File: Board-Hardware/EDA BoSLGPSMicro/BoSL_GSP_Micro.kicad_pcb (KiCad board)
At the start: 2 copper layers, 88 x 69.8 mm, 58 parts, among them CON1 Micro_SD_Card, CON2 BARREL_JACK, IC1 ATMEGA328-P, IC2 SIM7000, J1 Screw_Terminal_1x06, J2 Screw_Terminal_1x04, J3 Screw_Terminal_1x02, J4 Screw_Terminal_1x08, J5 Screw_Terminal_1x04, J6 RJ45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

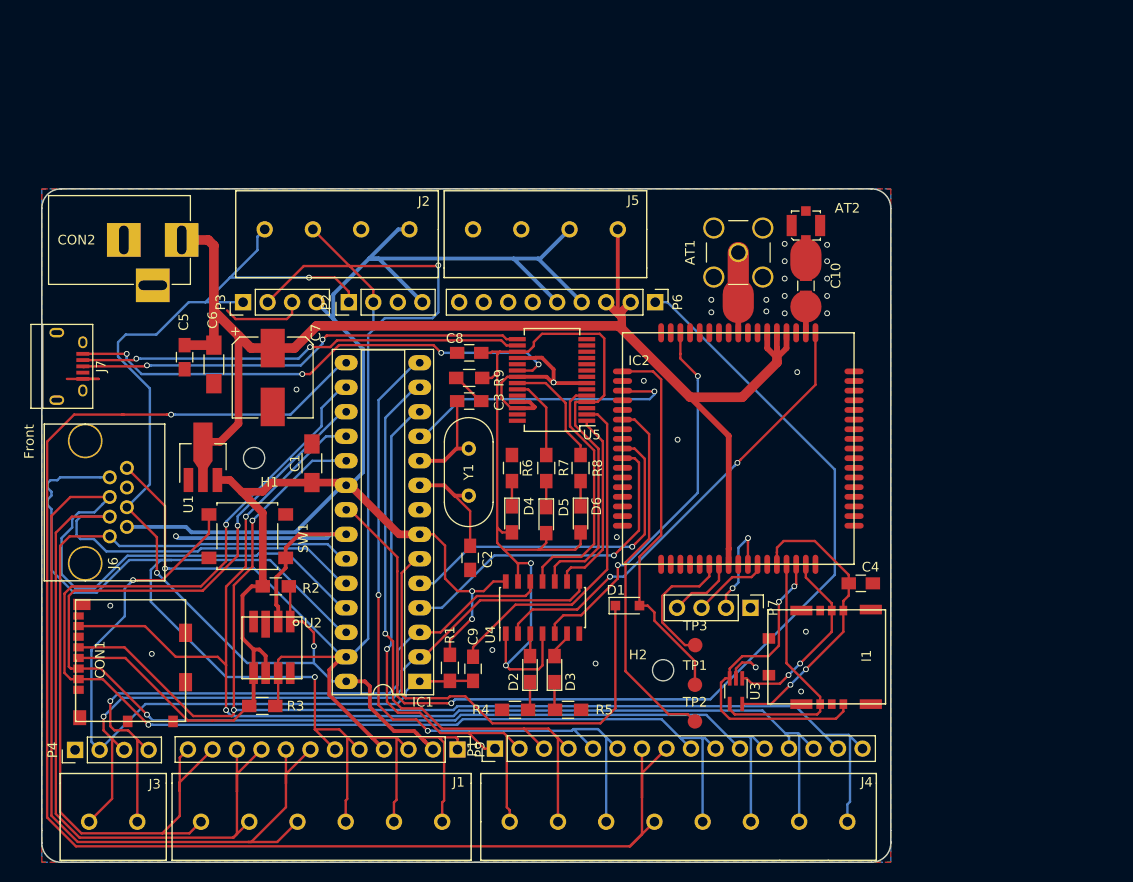
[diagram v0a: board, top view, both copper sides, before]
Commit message: started layout of micro bosl gps
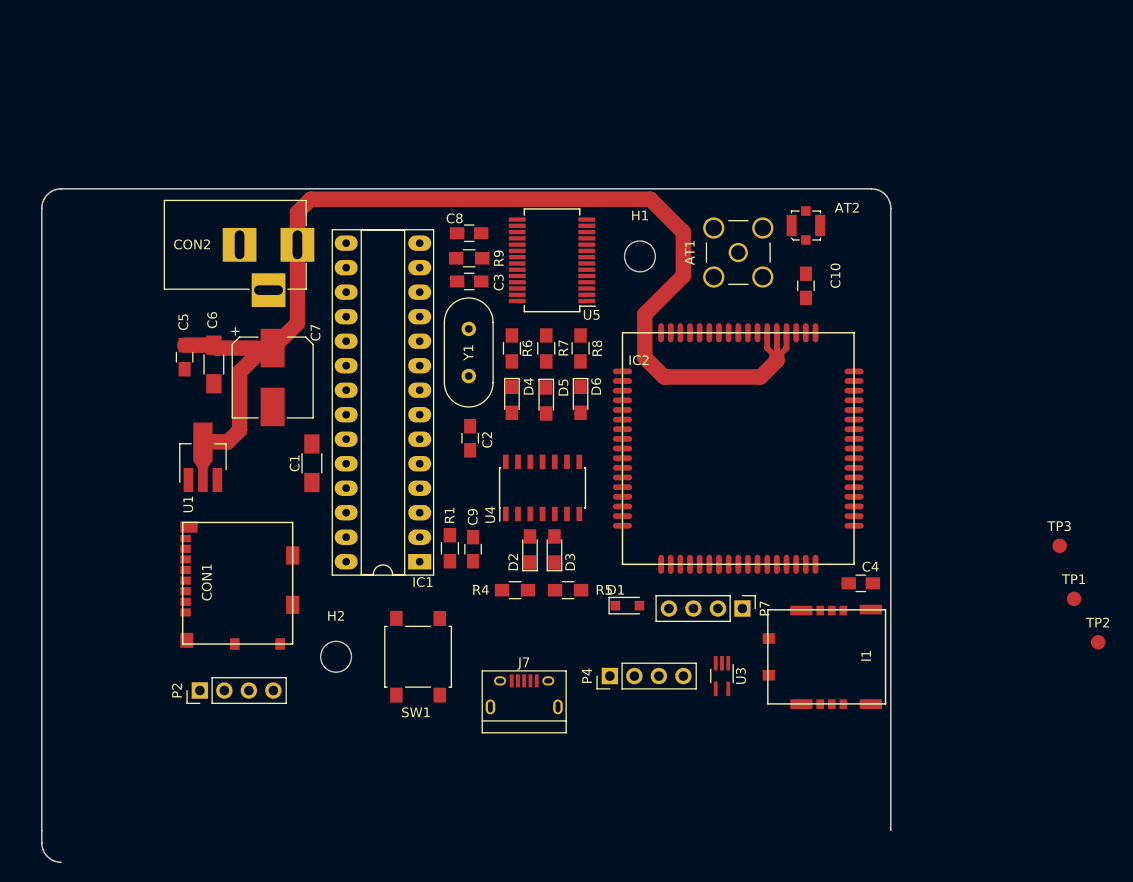
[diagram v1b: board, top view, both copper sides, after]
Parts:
- removed J1: Screw_Terminal_1x06, SIMFootprints:Screw_Terminals_1x6
- removed J2, J5: Screw_Terminal_1x04, SIMFootprints:Screw_Terminals_1x4
- removed J3: Screw_Terminal_1x02, SIMFootprints:Screw_Terminals_1x2
- removed J4: Screw_Terminal_1x08, SIMFootprints:Screw_Terminals_1x8
- removed J6: RJ45, SIMFootprints:RJ_45
- removed P1: CONN_01X16, Pin_Headers:Pin_Header_Straight_1x16_Pitch2.54mm
- removed P3: CONN_01X04, Pin_Headers:Pin_Header_Straight_1x04_Pitch2.54mm
- removed P6: CONN_01X09, Pin_Headers:Pin_Header_Straight_1x09_Pitch2.54mm
- removed P9: CONN_01X12, Pin_Headers:Pin_Header_Straight_1x12_Pitch2.54mm
- removed R2, R3: 10 kΩ, Resistors_SMD:R_0805_HandSoldering
- removed U2: MS5803, SIMFootprints:MS5803
- H1, H2: footprint Mounting_Holes:MountingHole_2.2mm_M2 -> Mounting_Holes:MountingHole_3.2mm_M3
- moved J7 58.1 mm to (154.5, 115.3), turned to 0 degrees
- moved P4 56.0 mm to (163.4, 113.5)
- moved H1 45.1 mm to (166.5, 70.0)
- moved P2 43.1 mm to (120.9, 115.0)
- moved TP2 42.6 mm to (214.0, 110.0)
- moved TP1 40.3 mm to (211.5, 105.5)
- moved TP3 39.2 mm to (210.0, 100.0)
- moved H2 33.9 mm to (135.0, 111.5)
- moved SW1 21.7 mm to (143.5, 111.5), turned to 90 degrees
- moved CON1 13.7 mm to (119.1, 103.8)
- moved C2 12.4 mm to (148.9, 88.8)
- moved C3 12.4 mm to (148.8, 72.6)
- moved C8 12.4 mm to (148.8, 67.6)
- moved C9 12.4 mm to (149.2, 100.3)
- moved D2 12.4 mm to (155.1, 100.4)
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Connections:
- IC1 pad 12: D6 -> (no net)
- IC1 pad 13: D7 -> (no net)
- IC1 pad 14: D8 -> (no net)
- IC1 pad 15: D9 -> (no net)
- IC1 pad 21: AREF -> (no net)
- IC1 pad 23: A0 -> (no net)
- IC1 pad 24: A1 -> (no net)
- IC1 pad 25: A2 -> (no net)
- IC1 pad 26: A3 -> (no net)
- J7 pad 6: (no net) -> Net-(J7-Pad6)
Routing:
- net V_3.3: track 198.8 -> 0.00 mm, vias 2 -> 0
- net D9: track 155.6 -> 0.00 mm, vias 1 -> 0
- net SDA: track 155.0 -> 0.00 mm, vias 2 -> 0
- net SD_MOSI: track 133.1 -> 0.00 mm, vias 2 -> 0
- net SD_SCLK: track 131.9 -> 0.00 mm, vias 2 -> 0
- net SD_CS: track 131.3 -> 0.00 mm, vias 2 -> 0
- net SCL: track 128.2 -> 0.00 mm, vias 3 -> 0
- net A2: track 128.0 -> 0.00 mm
- net SD_MISO: track 125.7 -> 0.00 mm, vias 2 -> 0
- net TTL_3.3V: track 110.1 -> 0.00 mm, vias 2 -> 0
- net AREF: track 109.6 -> 0.00 mm, vias 1 -> 0
- net A1: track 107.7 -> 0.00 mm
- net A3: track 101.4 -> 0.00 mm, vias 1 -> 0
- net A0: track 90.3 -> 0.00 mm
- net GND: track 76.1 -> 0.00 mm, vias 28 -> 0
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- removed copper zone on B.Cu, net GND
- removed copper zone on F.Cu, net GND
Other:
- outline, holes or cut-outs redrawn
- board text added: "Rev: 0.3 Gμ Monash BoSL GSP Micro Board"
- board text removed: "3.3V"
- board text removed: "A0"
- board text removed: "A1"
- board text removed: "A2"
- board text removed: "A3"
- board text removed: "A4"
- board text removed: "A5"
- board text removed: "AREF"
- board text removed: "D0"
- board text removed: "D1"
- board text removed: "D10"
- board text removed: "D11"
- board text removed: "D12"
- board text removed: "D13"
- board text removed: "D6"
- board text removed: "D7"
- board text removed: "D8"
- board text removed: "D9"
- board text removed: "DM"
- board text removed: "DP"
- board text removed: "GND"
- board text removed: "I2C"
- board text removed: "RESET"
- board text removed: "RX"
- board text removed: "Rev: 0.3 G Monash BoSL GSP Board"
- board text removed: "SCL"
- board text removed: "SD"
- board text removed: "SDA"
- board text removed: "TX"
- board text removed: "USB_DEBUG"
- board text removed: "V+"
- board text removed: "VPP"

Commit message: layout progress of gps micro board
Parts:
- removed IC1: ATMEGA328-P, Housings_DIP:DIP-28_W7.62mm_Socket_LongPads
- added U2: ATmega328P-AU, Housings_QFP:LQFP-32_7x7mm_Pitch0.8mm, F.Cu at (138.4, 85.9)
- moved TP2 45.6 mm to (190.8, 70.8)
- moved CON1 43.3 mm to (139.7, 65.7), turned to 180 degrees
- moved J7 38.9 mm to (118.0, 102.0), turned to 270 degrees
- moved TP3 38.2 mm to (190.8, 67.0)
- moved TP1 37.1 mm to (190.8, 74.8)
- moved I1 34.5 mm to (157.5, 109.2), turned to 0 degrees
- moved C9 29.4 mm to (164.0, 75.0)
- moved P4 22.2 mm to (141.9, 108.0)
- moved D1 20.1 mm to (150.0, 93.0)
- moved P2 18.5 mm to (138.0, 108.0), turned to 270 degrees
- moved SW1 15.6 mm to (133.0, 100.0), turned to 270 degrees
- moved R4 15.2 mm to (161.5, 91.7), turned to 270 degrees
- moved U4 14.3 mm to (143.0, 99.0), turned to 270 degrees
- moved R5 13.2 mm to (156.5, 91.7), turned to 270 degrees
- moved H2 11.9 mm to (125.0, 105.0), turned to 270 degrees
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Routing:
- net V_3.3: track 0.00 -> 101.6 mm
- net TTL_3.3V: track 0.00 -> 85.8 mm
- net TLL_RST: track 0.00 -> 80.7 mm, vias 0 -> 2
- net AND_TX: track 0.00 -> 74.7 mm, vias 0 -> 2
- net AND_RX: track 0.00 -> 63.2 mm, vias 0 -> 2
- net USB_DP: track 0.00 -> 62.9 mm, vias 0 -> 2
- net USB_DM: track 0.00 -> 60.0 mm, vias 0 -> 2
- net USB_V: track 0.00 -> 53.3 mm, vias 0 -> 2
- net NETLIGHT: track 0.00 -> 51.0 mm, vias 0 -> 2
- net PWR_STAT: track 0.00 -> 48.1 mm, vias 0 -> 2
- net Net-(C4-Pad2): track 0.00 -> 41.3 mm
- net Net-(I1-Pad3): track 0.00 -> 40.2 mm, vias 0 -> 2
- net Net-(I1-Pad6): track 0.00 -> 37.4 mm, vias 0 -> 2
- net RX: track 0.00 -> 33.2 mm, vias 0 -> 2
- net Net-(I1-Pad2): track 0.00 -> 32.8 mm, vias 0 -> 2
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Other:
- board size 88 x 69.8 mm -> 84 x 64.5 mm

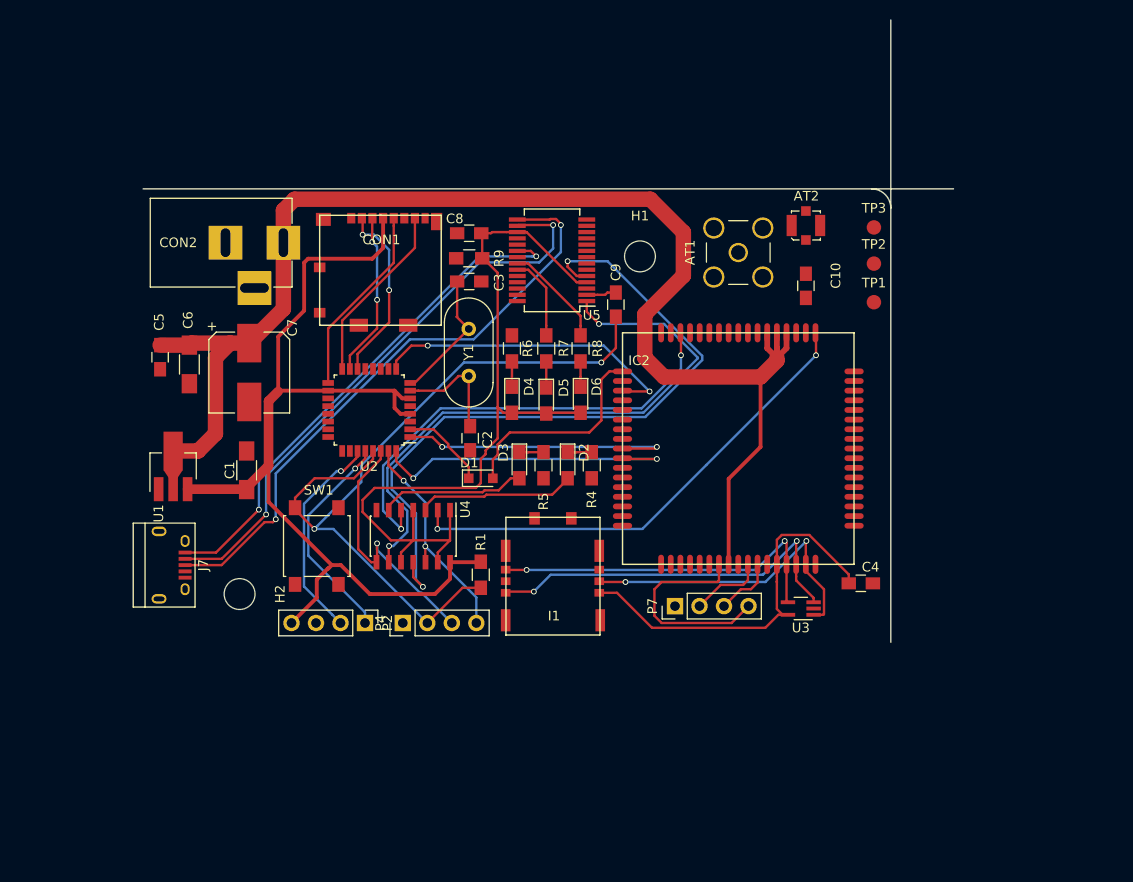
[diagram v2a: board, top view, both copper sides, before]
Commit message: finished initial layout of BoSL GPS micro
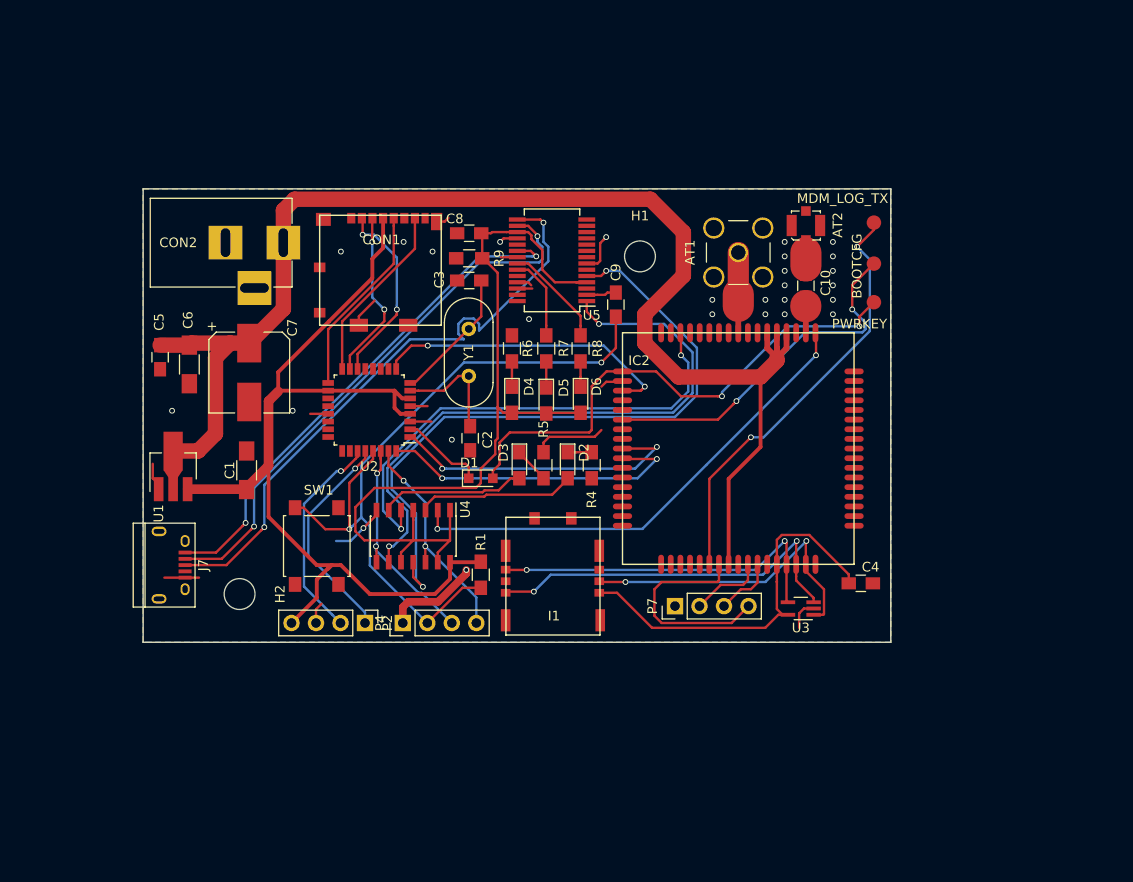
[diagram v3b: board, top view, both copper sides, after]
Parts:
- moved MDM_LOG_TX 0.50 mm to (190.8, 66.5)
- moved C3 0.10 mm to (148.8, 72.5), turned to 0 degrees
- turned R5 to 90 degrees
- renumbered TP2 to BOOTCFG, TP3 to MDM_LOG_TX, TP1 to PWRKEY
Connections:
- J7 pad 6: Net-(J7-Pad6) -> (no net)
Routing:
- net GND: track 0.00 -> 61.5 mm, vias 0 -> 27
- net Net-(IC2-Pad23): track 0.00 -> 44.4 mm, vias 0 -> 2
- net Net-(IC2-Pad6): track 0.00 -> 37.4 mm, vias 0 -> 2
- net Net-(D1-Pad2): track 22.3 -> 54.5 mm, vias 0 -> 2
- net Net-(AT1-Pad1): track 0.00 -> 9.60 mm
- net Net-(AT2-Pad1): track 0.00 -> 4.90 mm
- net TTL_3.3V: track 85.8 -> 90.5 mm
- net Net-(C10-Pad2): track 0.00 -> 3.76 mm
- net AND_TX: track 74.7 -> 71.1 mm
- net TLL_RX: track 27.1 -> 24.0 mm, vias 1 -> 2
- net VPP: track 142.6 -> 145.7 mm
- net V_3.3: track 101.6 -> 98.6 mm
- net USB_DM: track 60.0 -> 57.4 mm
- net PWR_STAT: track 48.1 -> 50.5 mm
- net TLL_RST: track 80.7 -> 78.3 mm
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- added copper zone on B.Cu, net GND
- added copper zone on F.Cu, net GND
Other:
- board size 84 x 64.5 mm -> 77.5 x 47 mm

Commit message: finished parts list for BoSL GPS Micro
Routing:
- net GND: track 61.5 -> 56.2 mm
- net USB_DP: track 63.5 -> 60.0 mm
- net TLL_RST: track 78.3 -> 81.2 mm
- net TTL_3.3V: track 90.5 -> 93.2 mm
- net TLL_TX: track 23.3 -> 25.6 mm
- net Net-(IC2-Pad6): track 37.4 -> 35.6 mm
- net AND_RX: track 64.5 -> 63.0 mm
- net AND_TX: track 71.1 -> 69.7 mm
- net PWR_STAT: track 50.5 -> 51.4 mm
- net DTR: track 31.5 -> 32.4 mm
- net Net-(D1-Pad2): track 54.5 -> 53.6 mm
- net SCL: track 22.7 -> 23.5 mm
- net Net-(C3-Pad2): track 13.9 -> 14.7 mm
- net NETLIGHT: track 51.0 -> 51.7 mm
- net Net-(IC2-Pad23): track 44.4 -> 45.0 mm
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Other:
- outline, holes or cut-outs redrawn
- board text added: "DM"
- board text added: "DP"
- board text added: "GND"
- board text added: "I2C"
- board text added: "RST"
- board text added: "RX"
- board text added: "SCL"
- board text added: "SDA"
- board text added: "TX"
- board text added: "USB_DEBUG"
- board text added: "V+"
- board text added: "V3.3"

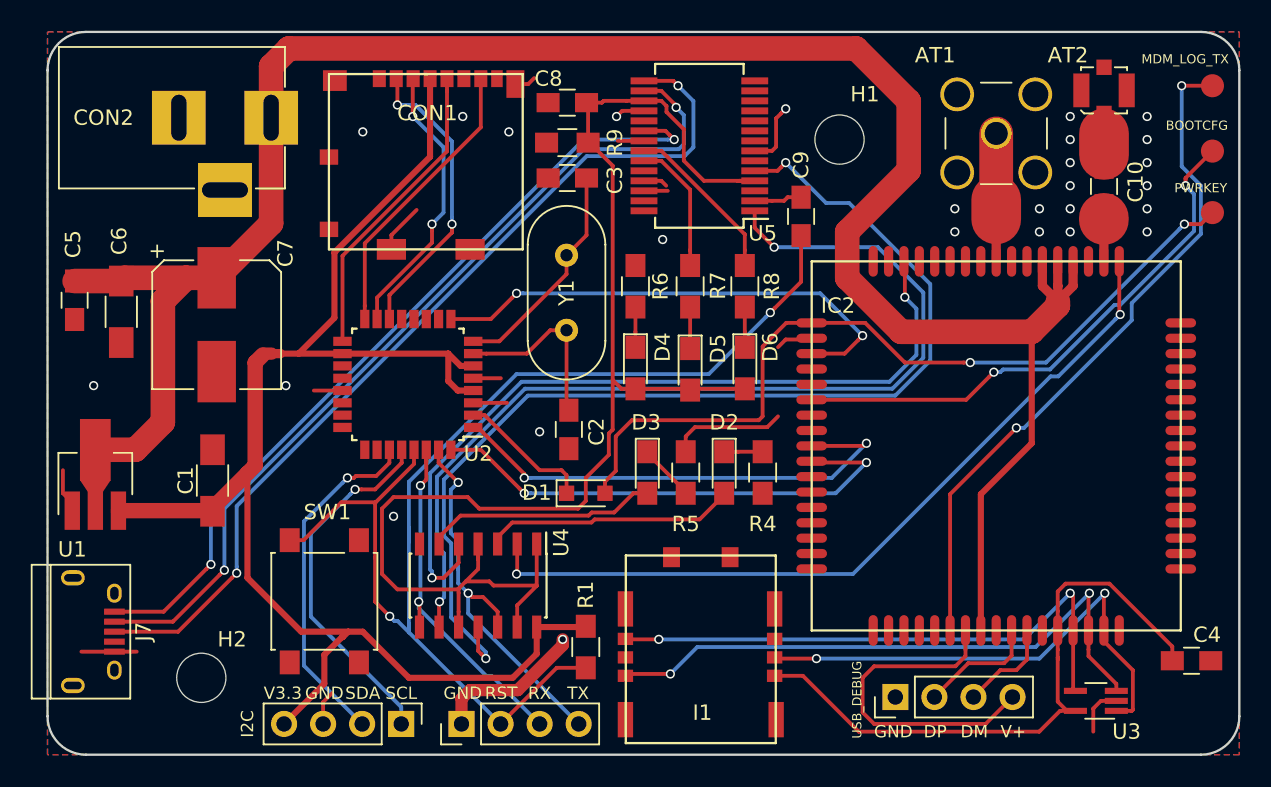
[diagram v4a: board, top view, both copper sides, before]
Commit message: added spi header to bosl GPS micro for bootloading
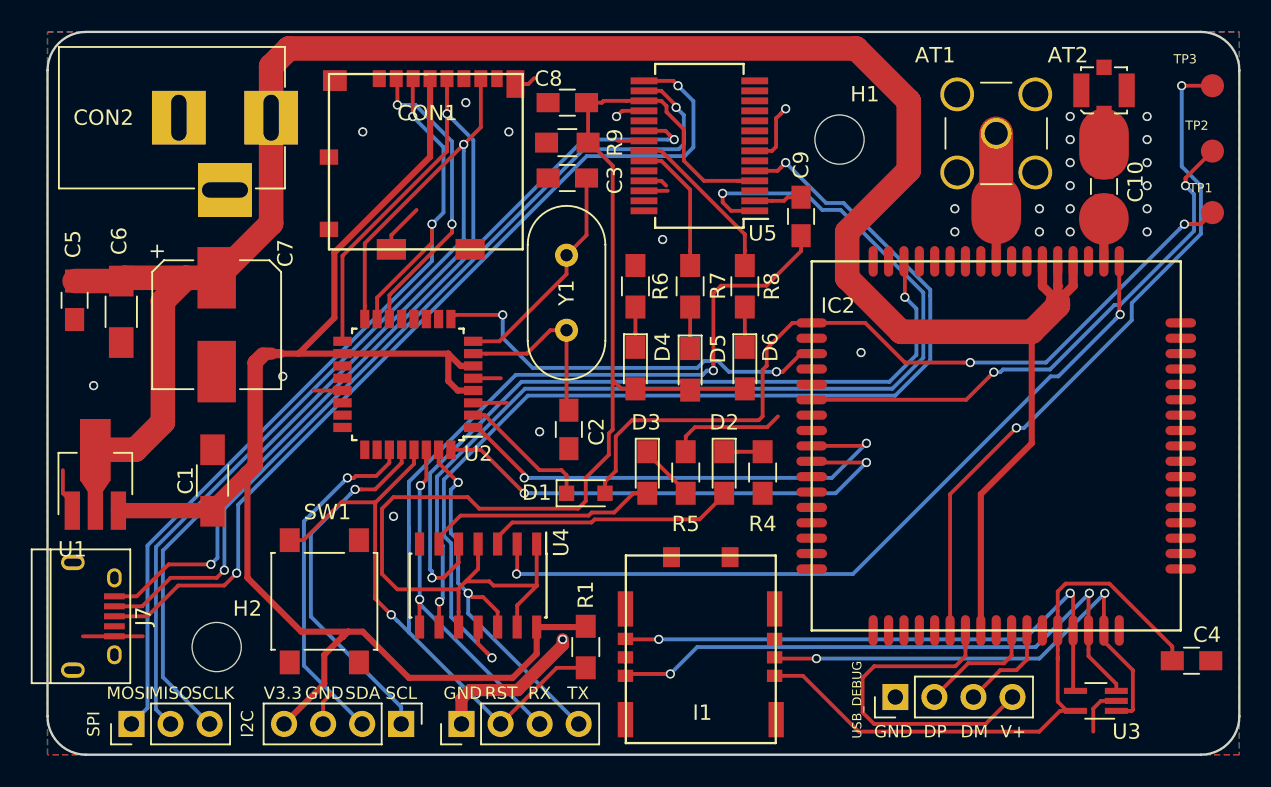
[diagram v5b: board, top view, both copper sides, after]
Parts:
- added J1: Conn_01x03, Pin_Headers:Pin_Header_Straight_1x03_Pitch2.54mm, F.Cu at (120.5, 108.0)
- moved H2 2.24 mm to (126.0, 103.0)
- moved J7 1.00 mm to (118.0, 101.0)
- renumbered PWRKEY to TP1, BOOTCFG to TP2, MDM_LOG_TX to TP3
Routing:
- net SD_SCLK: track 19.9 -> 69.9 mm, vias 0 -> 1
- net SD_MISO: track 18.8 -> 65.1 mm, vias 0 -> 1
- net SD_MOSI: track 18.3 -> 58.9 mm
- net DTR: track 32.4 -> 26.8 mm
- net AND_RX: track 63.0 -> 67.7 mm
- net TLL_RST: track 81.2 -> 82.8 mm
- net GND: track 56.2 -> 54.9 mm, vias 27 -> 28
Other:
- board text added: "MISO"
- board text added: "MOSI"
- board text added: "SCLK"
- board text added: "SPI"
